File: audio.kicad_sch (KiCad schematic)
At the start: 50 parts, among them J11 Gain Control, J12 Gain Control, J4 NCJ6FA-H-0, J5 NCJ6FA-H-0, Q2 MMBT3906, Q3 FFB3904, Q4 MMBT3906, Q5 FFB3904, U11 LM2903, U5 THAT1246, U6 THAT1246, U9 OPA1656ID

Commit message: output design update
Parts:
- added unit 2 of U11
- added unit 1 of U11
- added unit 2 of U9
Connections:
- net AUDIO_IN_L: now also U11.3 (+); no longer U11.3 (+)
- net AUDIO_IN_R: now also U11.5 (+); no longer U11.5 (+)
- net GND: now also U9.5 (+); no longer U9.5 (+)
- net L_Clip_Led: now also U11.1; no longer U11.1
- net R_Clip_Led: now also U11.7; no longer U11.7
- net R_Gain_A: now also U9.6 (-); no longer U9.6 (-)
- net R_Gain_B: now also U9.7; no longer U9.7
- net at RV2.2: now also U11.6 (-); no longer U11.6 (-)
- net at RV1.2: now also U11.2 (-); no longer U11.2 (-)
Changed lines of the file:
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@@
 	)
 	(junction
-		(at 82.55 125.73)
-		(diameter 0)
-		(color 0 0 0 0)
-	)
-	(junction
 		(at 76.2 180.34)
 		(diameter 0)
@@
 	)
 	(junction
-		(at 91.44 125.73)
+		(at 82.55 125.73)
 		(diameter 0)
 		(color 0 0 0 0)
@@
 	(wire
 		(pts
-			(xy 82.55 125.73) (xy 82.55 120.65)
-		)
-		(stroke
-			(width 0)
-			(type default)
-		)
-	)
-	(wire
-		(pts
 			(xy 142.24 48.26) (xy 142.24 53.34)
 		)
@@
 	(wire
 		(pts
+			(xy 83.82 125.73) (xy 82.55 125.73)
+		)
+		(stroke
+			(width 0)
+			(type default)
+		)
+	)
+	(wire
+		(pts
 			(xy 176.53 111.76) (xy 179.07 111.76)
 		)
@@
 	(wire
 		(pts
-			(xy 82.55 128.27) (xy 82.55 125.73)
+			(xy 82.55 120.65) (xy 82.55 125.73)
 		)
 		(stroke
@@
 	(wire
 		(pts
-			(xy 82.55 125.73) (xy 83.82 125.73)
-		)
-		(stroke
-			(width 0)
-			(type default)
-		)
-	)
-	(wire
-		(pts
 			(xy 55.88 128.27) (xy 57.15 128.27)
 		)
@@
 	(wire
 		(pts
-			(xy 90.17 125.73) (xy 91.44 125.73)
-		)
-		(stroke
-			(width 0)
-			(type default)
-		)
-	)
-	(wire
-		(pts
 			(xy 55.88 116.84) (xy 55.88 99.06)
 		)
@@
 	(wire
 		(pts
+			(xy 82.55 125.73) (xy 82.55 128.27)
+		)
+		(stroke
+			(width 0)
+			(type default)
+		)
+	)
+	(wire
+		(pts
 			(xy 88.9 90.17) (xy 88.9 85.09)
 		)
@@
 			)
 		)
-		(property "Description" "Potentiometer"
+		(property "Description" "Potentiometer - Audio Taper"
 			(at 207.01 144.78 0)
 			(effects
@@
 			)
 		)
-		(property "Description" "Potentiometer"
+		(property "Description" "Potentiometer - Audio Taper"
 			(at 184.15 144.78 0)
 			(effects

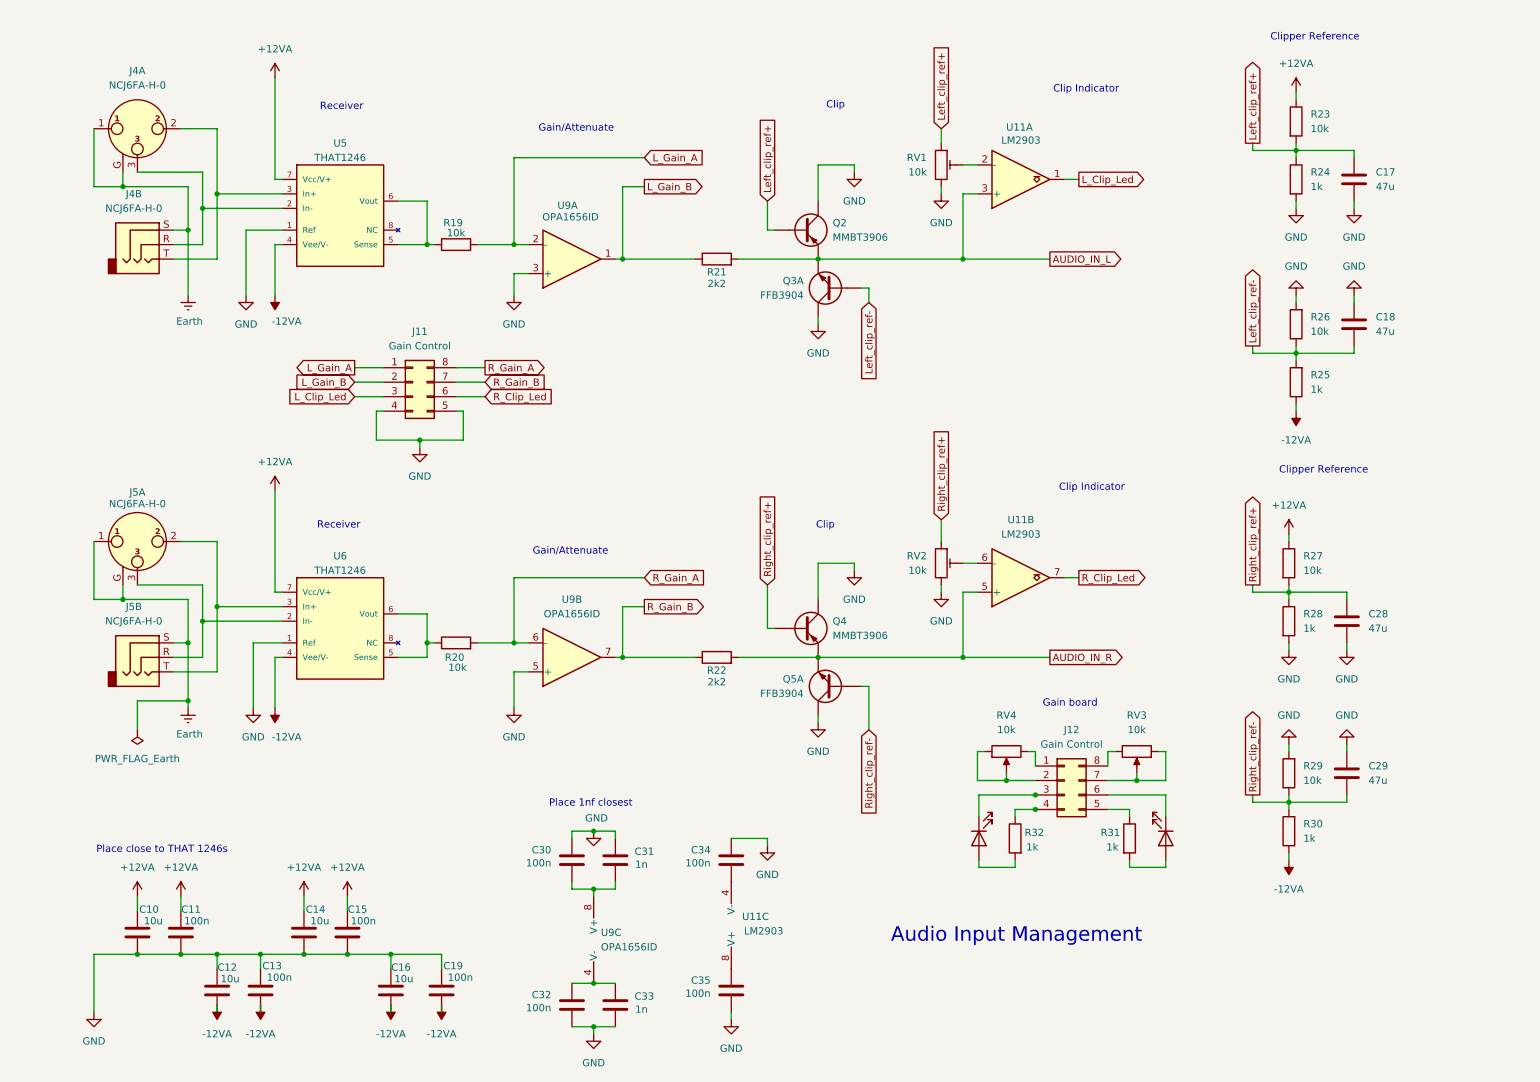
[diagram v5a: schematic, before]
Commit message: Cleanup and review of input pt 1
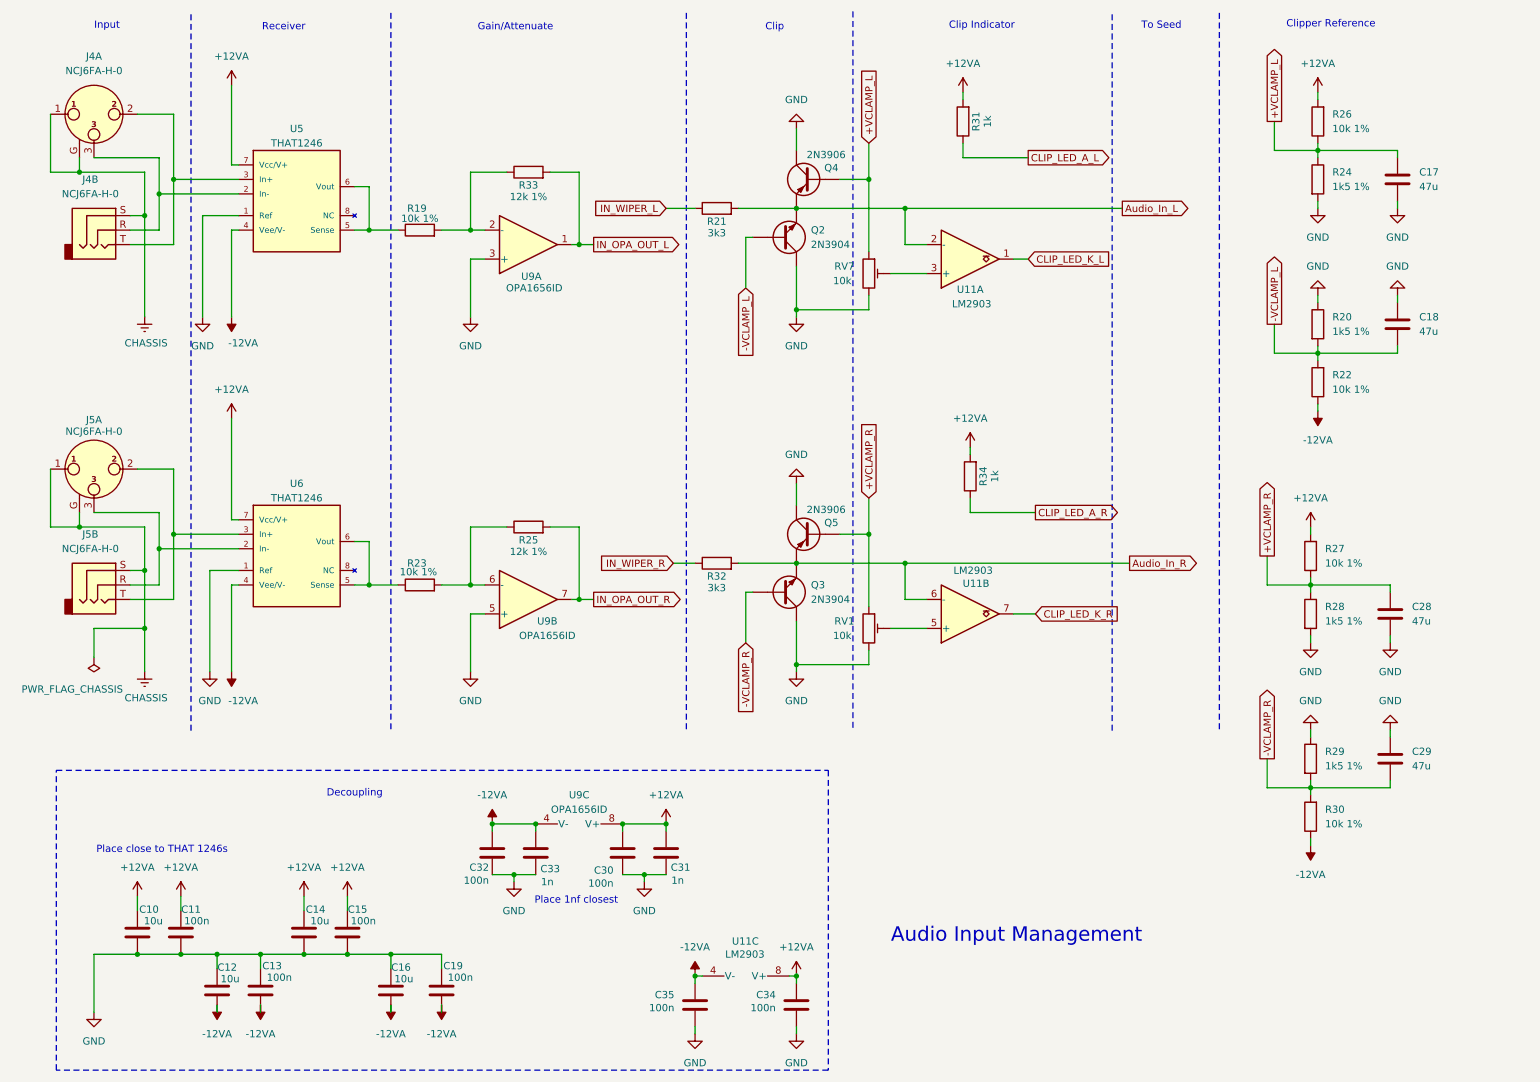
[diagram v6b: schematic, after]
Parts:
- removed D2, D4: LED, symbol Device:LED
- removed J11, J12: Gain Control, symbol Connector_Generic:Conn_02x04_Counter_Clockwise
- removed Q2, Q4: MMBT3906, Package_TO_SOT_SMD:SOT-23, symbol Transistor_BJT:MMBT3906
- removed Q3, Q5: FFB3904, Package_TO_SOT_SMD:SOT-363_SC-70-6, symbol Transistor_BJT:FFB3904
- removed RV2: 10k, symbol Device:R_Potentiometer_Trim
- removed RV3, RV4: 10k, symbol Device:R_Potentiometer
- removed unit 2 of U11
- added Q2, Q3: 2N3904, Package_TO_SOT_SMD:SOT-23, symbol Transistor_BJT:2N3904
- added Q4, Q5: 2N3906, Package_TO_SOT_SMD:SOT-23, symbol Transistor_BJT:2N3906
- added R33: 12k 1%, symbol Device:R
- added R34: 1k, symbol Device:R
- added RV7: 10k, symbol Device:R_Potentiometer_Trim
- added unit 1 of U11
- R19, R26, R27: value 10k -> 10k 1%
- R20: value 10k -> 1k5 1%; footprint Resistor_SMD:R_0603_1608Metric -> (none); Placement In signal path between THAT1246 output and protection diode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 -> (none)
- R21: value 2k2 -> 3k3
- R22: value 2k2 -> 10k 1%
- R23: value 10k -> 10k 1%; footprint (none) -> Resistor_SMD:R_0603_1608Metric; Placement (none) -> In signal path between THAT1246 output and protection diode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
- R24, R28: value 1k -> 1k5 1%
- R25: value 1k -> 12k 1%
- R29: value 10k -> 1k5 1%
- R30: value 1k -> 10k 1%
- R32: value 1k -> 3k3
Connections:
- net +12VA: now also C30.1, C31.1, C34.1, R26.2, R27.2, R31.2, U11.8 (V+), U9.8 (V+), R34.2; no longer R23.1, R27.1
- net -12VA: now also C32.1, C33.1, C35.1, R22.1, U11.4 (V-), U9.4 (V-); no longer R25.1
- net GND: now also C30.2, C31.2, C34.2, R20.1, R29.1, Q2.3 (C), Q3.3 (C), Q4.3 (C), Q5.3 (C), RV7.3; no longer C30.1, C31.1, C34.1, R26.2, R29.2
- net Audio_In_R: now reaches R32.2
- net Audio_In_R: now also U11.6 (-), Q3.1 (E), Q5.1 (E)
- net IN_WIPER_R: now reaches R32.1
- net CLIP_LED_A_L: now reaches R31.1
- net at RV1.2: now also U11.5 (+); no longer U11.2 (-)
- net at U6.5 (Sense), U6.6 (Vout): now also R23.1; no longer R20.1
- net AUDIO_IN_L renamed Audio_In_L
- net Audio_In_L: now also Q2.1 (E), Q4.1 (E), U11.2 (-); no longer U11.3 (+)
- net AUDIO_IN_R renamed -VCLAMP_L
- net -VCLAMP_L: now also C18.2, R20.2, Q2.2 (B)
- net Earth renamed CHASSIS
- removed net L_Clip_Led: U11.1
- net L_Gain_A: no longer names the net of R19.2, U9.2 (-)
- net L_Gain_A: now also R33.1
- net L_Gain_B renamed IN_OPA_OUT_L
- net IN_OPA_OUT_L: now also R33.2; no longer R21.1
- net Left_clip_ref+ renamed +VCLAMP_L
- net +VCLAMP_L: now also R26.1, Q4.2 (B), RV7.1; no longer R23.2, RV1.1
- removed net Left_clip_ref-: C18.2, R25.2, R26.1
- net R_Gain_A: no longer names the net of U9.6 (-)
- net R_Gain_A: now also R23.2, R25.1; no longer R20.2
- net R_Gain_B renamed IN_OPA_OUT_R
- net IN_OPA_OUT_R: now also R25.2; no longer R22.1
- net Right_clip_ref+ renamed +VCLAMP_R
- net +VCLAMP_R: now also R27.1, RV1.1, Q5.2 (B); no longer R27.2
- net Right_clip_ref- renamed -VCLAMP_R
- net -VCLAMP_R: now also R29.2, Q3.2 (B); no longer R29.1
- new net: RV7.2, U11.3 (+)
- new net CLIP_LED_A_R: R34.1
- new net CLIP_LED_K_L: U11.1
- new net CLIP_LED_K_R: U11.7
- new net IN_WIPER_L: R21.1
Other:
- note added: "Decoupling"
- note added: "Input"
- note added: "To Seed"
- note removed: "Gain board"
- moved on the sheet: C17, C18, C30, C31, C32, C33, C34, C35, J4A, J4B, J5A, J5B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

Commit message: fix some footprints
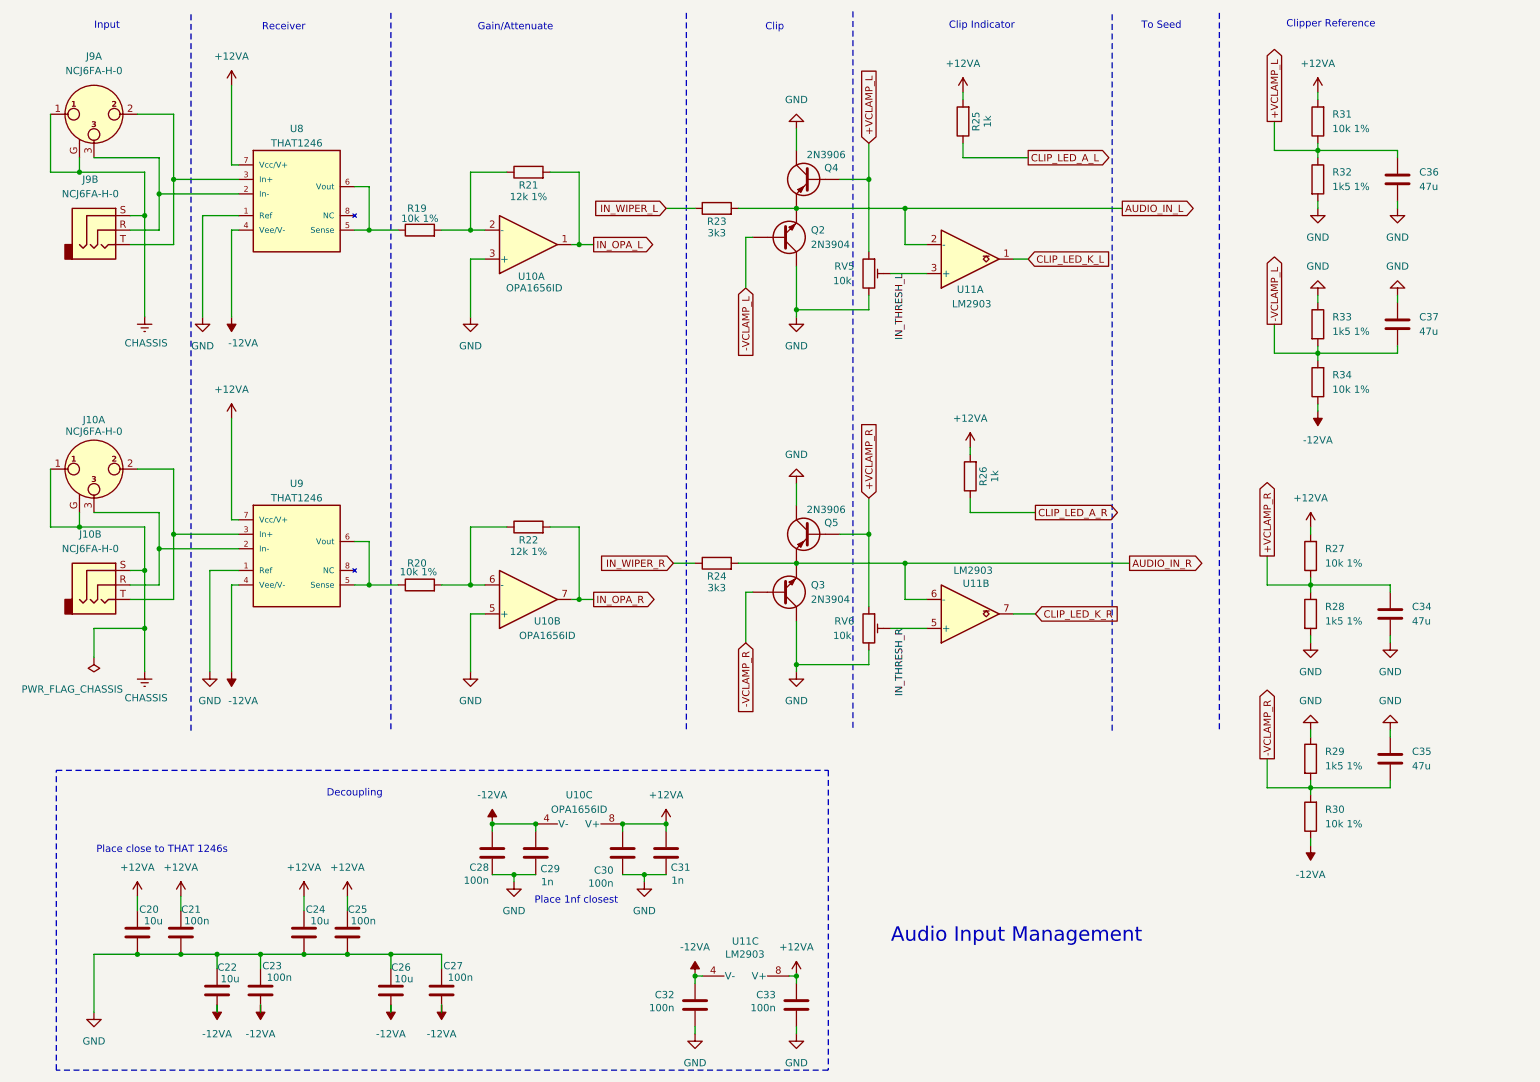
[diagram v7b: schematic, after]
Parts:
- C34: renamed from C28; footprint (none) -> Capacitor_SMD:C_1206_3216Metric
- C35: renamed from C29; footprint (none) -> Capacitor_SMD:C_1206_3216Metric
- C36: renamed from C17; footprint (none) -> Capacitor_SMD:C_1206_3216Metric
- C37: renamed from C18; footprint (none) -> Capacitor_SMD:C_1206_3216Metric
- R19: footprint Resistor_SMD:R_0603_1608Metric -> Resistor_SMD:R_0805_2012Metric
- R20: renamed from R23; footprint Resistor_SMD:R_0603_1608Metric -> Resistor_SMD:R_0805_2012Metric
- R21: renamed from R33; footprint (none) -> Resistor_SMD:R_0805_2012Metric
- R22: renamed from R25; footprint (none) -> Resistor_SMD:R_0805_2012Metric
- R23: renamed from R21; footprint (none) -> Resistor_SMD:R_0805_2012Metric
- R24: renamed from R32; footprint (none) -> Resistor_SMD:R_0805_2012Metric
- R25: renamed from R31; footprint (none) -> Resistor_SMD:R_0805_2012Metric
- R26: renamed from R34; footprint (none) -> Resistor_SMD:R_0805_2012Metric
- R27, R28, R29, R30: footprint (none) -> Resistor_SMD:R_0805_2012Metric
- R31: renamed from R26; footprint (none) -> Resistor_SMD:R_0805_2012Metric
- R32: renamed from R24; footprint (none) -> Resistor_SMD:R_0805_2012Metric
- R33: renamed from R20; footprint (none) -> Resistor_SMD:R_0805_2012Metric
- R34: renamed from R22; footprint (none) -> Resistor_SMD:R_0805_2012Metric
- renumbered C10 to C20, C11 to C21, C12 to C22, C13 to C23, C14 to C24, C15 to C25, C16 to C26, C19 to C27, C32 to C28, C33 to C29, C35 to C32, C34 to C33, J5 to J10, J4 to J9, RV7 to RV5, RV1 to RV6, U9 to U10, U5 to U8, U6 to U9
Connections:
- net IN_THRESH_R: now reaches RV6.2, U11.5 (+)
- net IN_THRESH_L: now reaches RV5.2, U11.3 (+)
- net Audio_In_L renamed AUDIO_IN_L
- net Audio_In_R renamed AUDIO_IN_R
- net IN_OPA_OUT_L renamed IN_OPA_L
- net IN_OPA_OUT_R renamed IN_OPA_R
